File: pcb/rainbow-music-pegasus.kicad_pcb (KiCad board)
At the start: 2 copper layers, 138 x 30.5 mm, 88 parts, among them J1 USB_B_Micro, J2 Conn_02x03_Odd_Even, SW1 SW_SPDT, U1 ESP32-C3-MINI-1, U2 OPA344NA, U3 TLV75533PDBV

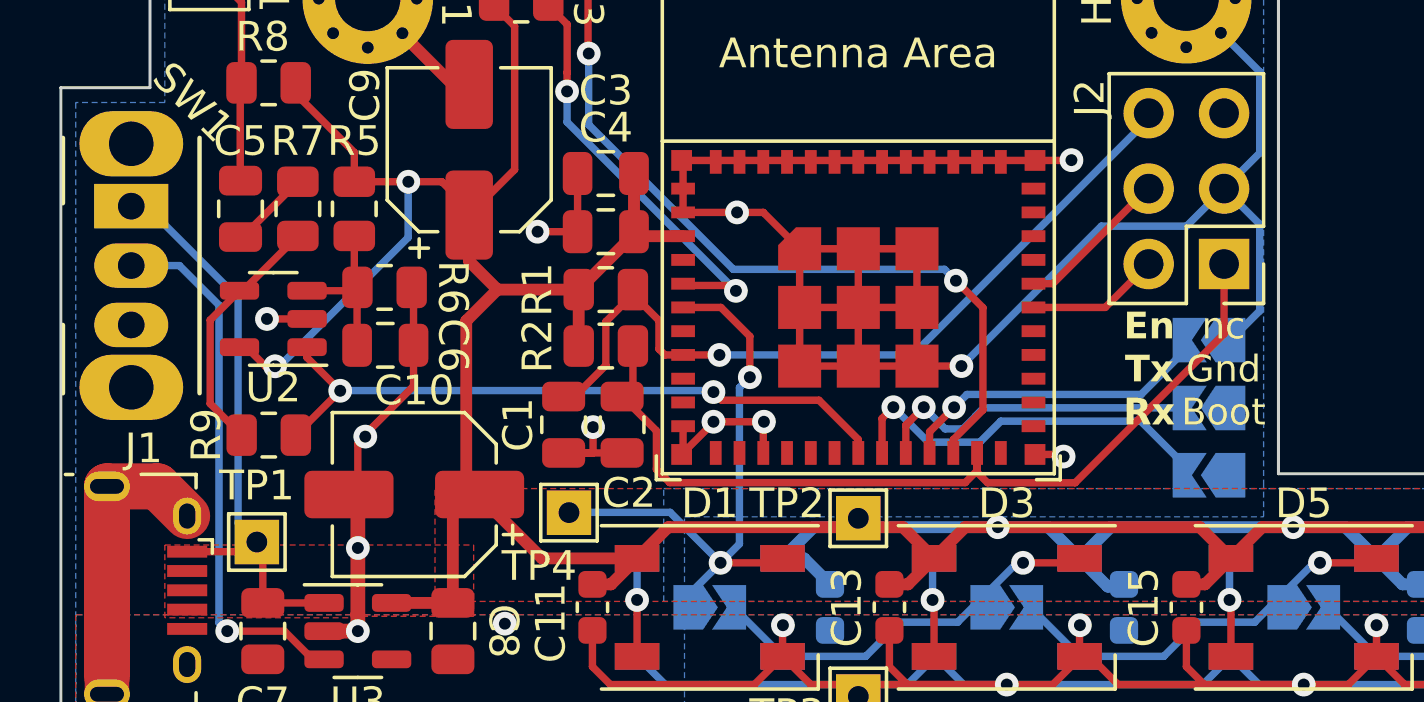
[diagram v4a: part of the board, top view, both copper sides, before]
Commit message: Missed a decoupling capacitor at U2; added as C35
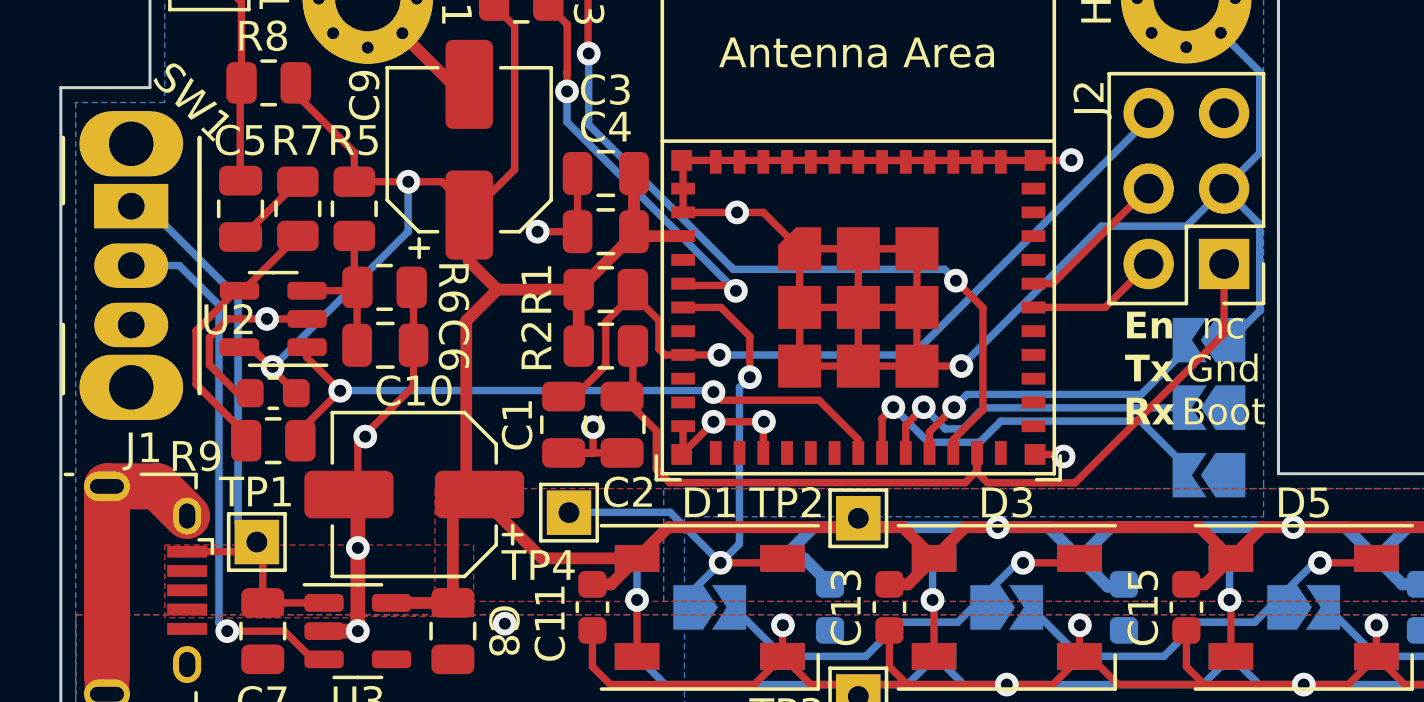
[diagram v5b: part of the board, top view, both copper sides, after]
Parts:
- added C35: 0.1uF, Capacitor_SMD:C_0603_1608Metric, F.Cu at (91.1, 93.4)
- moved R9 0.24 mm to (91.1, 95.0)
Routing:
- net GND: track 413.6 -> 418.5 mm
- net +3.3V: track 351.1 -> 352.2 mm

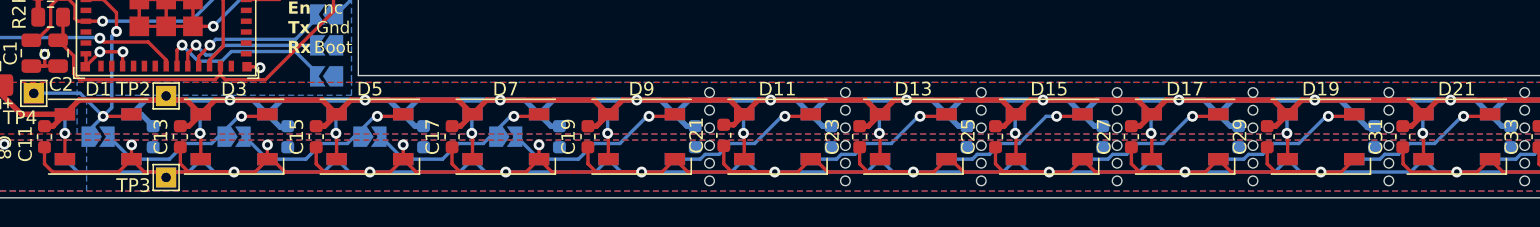
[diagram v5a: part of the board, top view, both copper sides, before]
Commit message: Footprint verification done, ready for first production run!
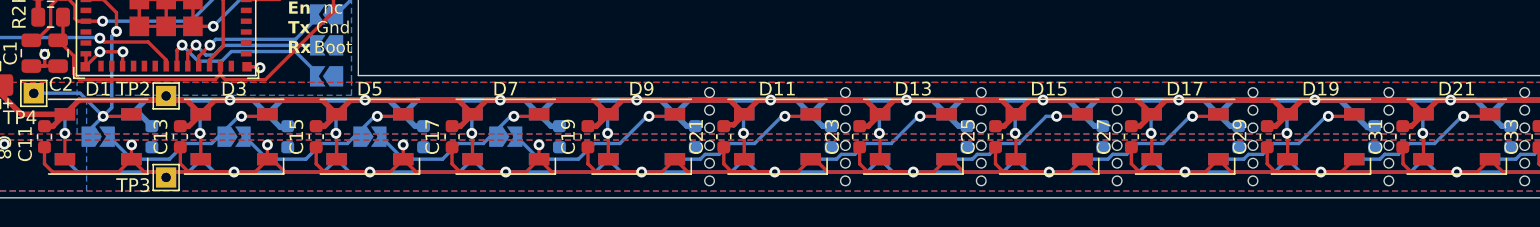
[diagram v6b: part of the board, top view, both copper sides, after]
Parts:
- moved C12 0.10 mm to (109.7, 100.6)
- moved C21 0.10 mm to (151.8, 100.6)
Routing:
- net GND: track 418.5 -> 428.5 mm
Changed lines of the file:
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@@
     )
     (pad_to_mask_clearance 0)
-    (grid_origin 95.8475 96.8)
+    (grid_origin 119.7475 100.6)
     (pcbplotparams
       (layerselection 0x00010fc_ffffffff)
@@
   )
   (footprint "Capacitor_SMD:C_0603_1608Metric" (layer "F.Cu")
-    (at 151.8475 100.5 90)
+    (at 151.8475 100.6 90)
     (descr "Capacitor SMD 0603 (1608 Metric), square (rectangular) end terminal, IPC_7351 nominal, (Body size source: IPC-SM-782 page 76, https://www.pcb-3d.com/wordpress/wp-content/uploads/ipc-sm-782a_amendment_1_and_2.pdf), generated with kicad-footprint-generator")
     (tags "capacitor")
@@
   )
   (footprint "Jumper:SolderJumper-2_P1.3mm_Open_TrianglePad1.0x1.5mm" (layer "B.Cu")
-    (at 105.7975 100.6)
+    (at 105.8 100.6)
     (descr "SMD Solder Jumper, 1x1.5mm Triangular Pads, 0.3mm gap, open")
     (tags "solder jumper open")
@@
   )
   (footprint "Capacitor_SMD:C_0603_1608Metric" (layer "B.Cu")
-    (at 109.8475 100.6 90)
+    (at 109.7475 100.6 90)
     (descr "Capacitor SMD 0603 (1608 Metric), square (rectangular) end terminal, IPC_7351 nominal, (Body size source: IPC-SM-782 page 76, https://www.pcb-3d.com/wordpress/wp-content/uploads/ipc-sm-782a_amendment_1_and_2.pdf), generated with kicad-footprint-generator")
     (tags "capacitor")
@@
   (segment (start 138.25 101.200498) (end 138.25 102.25) (width 0.25) (layer "F.Cu") (net 1))
   (segment (start 131.8475 101.375) (end 131.8475 102.5975) (width 0.25) (layer "F.Cu") (net 1))
+  (segment (start 195.8 103.2) (end 205.8 103.2) (width 0.25) (layer "F.Cu") (net 1))
   (segment (start 132.45 103.2) (end 135.8 103.2) (width 0.25) (layer "F.Cu") (net 1))
   (segment (start 104.85 85.55) (end 116.75 85.55) (width 0.25) (layer "F.Cu") (net 1))
@@
   (segment (start 147.2 97.9) (end 148.25 98.95) (width 0.4) (layer "B.Cu") (net 4))
   (segment (start 149.3 97.9) (end 150.71303 97.9) (width 0.4) (layer "B.Cu") (net 4))
-  (segment (start 109.8475 99.825) (end 108.9725 98.95) (width 0.4) (layer "B.Cu") (net 4))
   (segment (start 199.225 99.925) (end 198.25 98.95) (width 0.4) (layer "B.Cu") (net 4))
   (segment (start 179.3 97.9) (end 180.71303 97.9) (width 0.4) (layer "B.Cu") (net 4))
@@
   (segment (start 157.2 97.9) (end 158.25 98.95) (width 0.4) (layer "B.Cu") (net 4))
   (segment (start 170.71303 97.9) (end 170.776699 97.91335) (width 0.4) (layer "B.Cu") (net 4))
-  (segment (start 108.9725 98.95) (end 108.25 98.95) (width 0.4) (layer "B.Cu") (net 4))
   (segment (start 167.2 97.9) (end 168.25 98.95) (width 0.4) (layer "B.Cu") (net 4))
   (segment (start 179.7475 99.825) (end 179.125 99.825) (width 0.4) (layer "B.Cu") (net 4))
@@
   (segment (start 168.25 98.95) (end 169.3 97.9) (width 0.4) (layer "B.Cu") (net 4))
   (segment (start 215.3475 97.9) (end 210.883805 97.9) (width 0.4) (layer "B.Cu") (net 4))
+  (segment (start 109.75 99.825) (end 108.875 98.95) (width 0.4) (layer "B.Cu") (net 4))
   (segment (start 200.883805 97.9) (end 200.776699 97.91335) (width 0.4) (layer "B.Cu") (net 4))
   (segment (start 149.7475 99.825) (end 149.125 99.825) (width 0.4) (layer "B.Cu") (net 4))
@@
   (segment (start 119.7475 99.825) (end 119.7475 99.9) (width 0.4) (layer "B.Cu") (net 4))
   (segment (start 187.2 97.9) (end 188.25 98.95) (width 0.4) (layer "B.Cu") (net 4))
+  (segment (start 108.875 98.95) (end 108.25 98.95) (width 0.4) (layer "B.Cu") (net 4))
   (segment (start 150.71303 97.9) (end 150.776699 97.91335) (width 0.4) (layer "B.Cu") (net 4))
   (segment (start 207.2 97.9) (end 208.25 98.95) (width 0.4) (layer "B.Cu") (net 4))

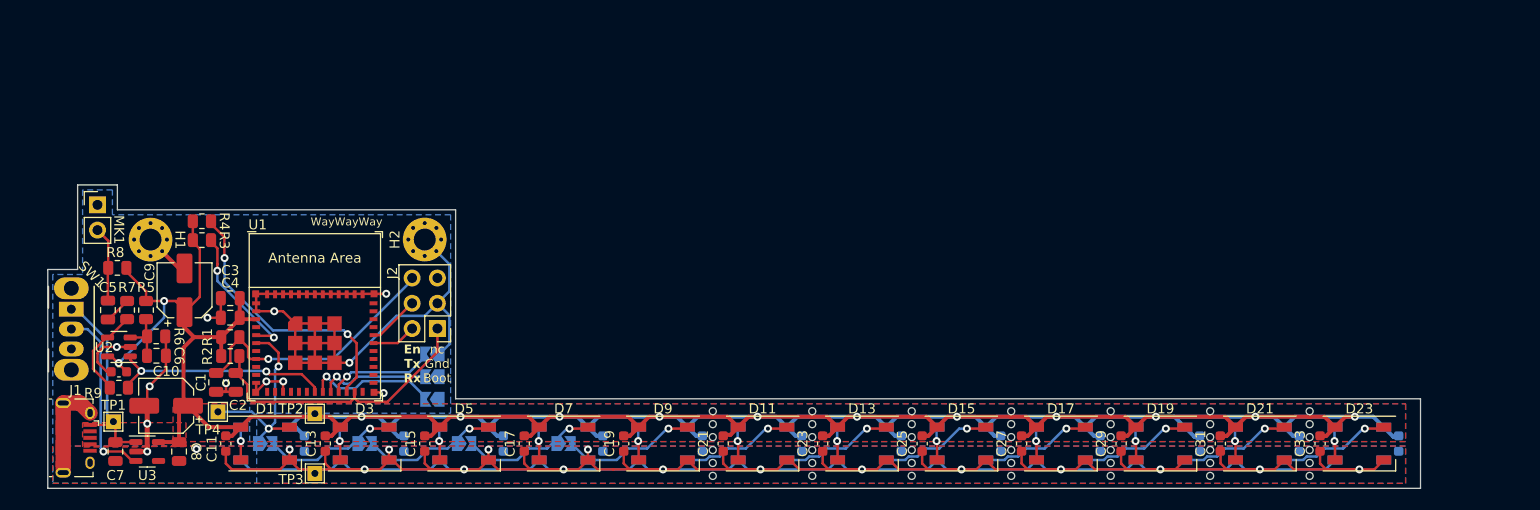
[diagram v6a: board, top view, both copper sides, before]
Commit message: Added Battery charging module and a new mode-setting button
Also found 3d models for the microphone, switch, USB components
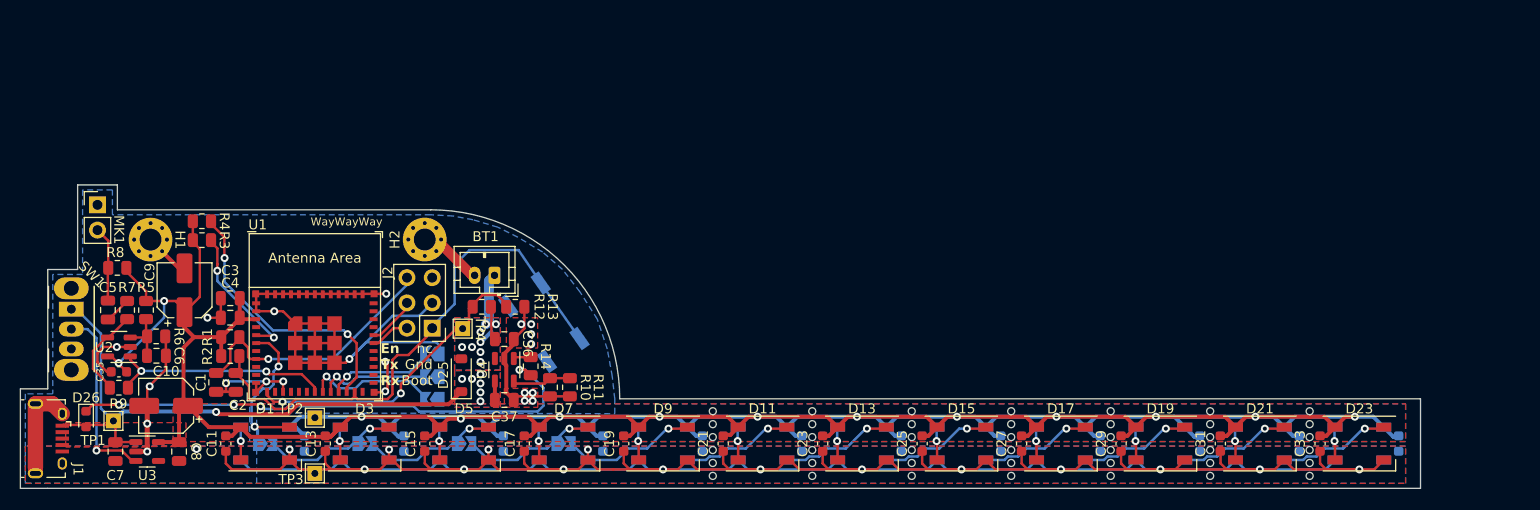
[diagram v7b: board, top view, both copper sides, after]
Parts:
- added BT1: Battery_Cell, Connector_JST:JST_PH_B2B-PH-K_1x02_P2.00mm_Vertical, F.Cu at (128.9, 83.7)
- added C36: 4.7uF, Capacitor_SMD:C_0805_2012Metric, F.Cu at (129.8, 90.1)
- added C37: 4.7uF, Capacitor_SMD:C_0805_2012Metric, F.Cu at (129.8, 96.2)
- added D25: MBR120, Diode_SMD:D_SOD-123, F.Cu at (125.5, 93.7)
- added D26: LED, LED_SMD:LED_0603_1608Metric, F.Cu at (87.8, 98.1)
- added R10: 10k, Resistor_SMD:R_0805_2012Metric, F.Cu at (134.4, 94.9)
- added R11: 10k, Resistor_SMD:R_0805_2012Metric, F.Cu at (136.4, 94.9)
- added R12: 100k, Resistor_SMD:R_0805_2012Metric, F.Cu at (127.6, 86.8)
- added R13: 100k, Resistor_SMD:R_0805_2012Metric, F.Cu at (130.9, 86.8)
- added R14: 1k, Resistor_SMD:R_0805_2012Metric, F.Cu at (132.5, 92.8)
- added SW2: SW_Push, Button_Switch_SMD:SW_SPST_EVQQ2, B.Cu at (133.8, 88.4)
- added U4: MCP73831-2-OT, Package_TO_SOT_SMD:SOT-23-5, F.Cu at (129.8, 93.2)
- moved TP4 26.0 mm to (125.7, 89.0)
- moved J1 2.79 mm to (83.9, 100.1)
- moved J2 0.52 mm to (122.6, 89.0)
- moved TP2 0.40 mm to (110.8, 98.0)
- moved TP1 0.08 mm to (90.5, 98.3)
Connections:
- net Net-(J1-VBUS) renamed VBUS
- TP4 pad 1: /RGB_Data -> /Batt_Level
- U1 pad 12: unconnected-(U1-GPIO0/ADC1_CH0/XTAL_32K_P-Pad12) -> /Batt_Level
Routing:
- net Net-(D26-K): track 0.00 -> 53.3 mm, vias 0 -> 4
- net VBUS: track 19.9 -> 61.1 mm, vias 0 -> 7
- net /Batt_Level: track 0.00 -> 31.1 mm, vias 0 -> 2
- net GND: track 428.5 -> 455.3 mm, vias 28 -> 37
- net /Boot: track 30.1 -> 55.7 mm
- net +BATT: track 0.00 -> 11.4 mm, vias 0 -> 8
- net Net-(U4-PROG): track 0.00 -> 5.97 mm
- net /RGB_Data: track 20.6 -> 17.1 mm
- net Net-(U4-STAT): track 0.00 -> 1.76 mm
- net /Reset: track 27.2 -> 27.8 mm
- net /RXD: track 4.48 -> 3.98 mm
- added copper zone on B.Cu, net +BATT
- added copper zone on F.Cu, net +BATT
- added copper zone on B.Cu, net VBUS
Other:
- board size 138 x 30.5 mm -> 140.8 x 30.5 mm
- board text added: "Set Mode (See website)"
- board text added: "v1.1"
- board text removed: "v1"

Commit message: Finalized battery design including charging status lights
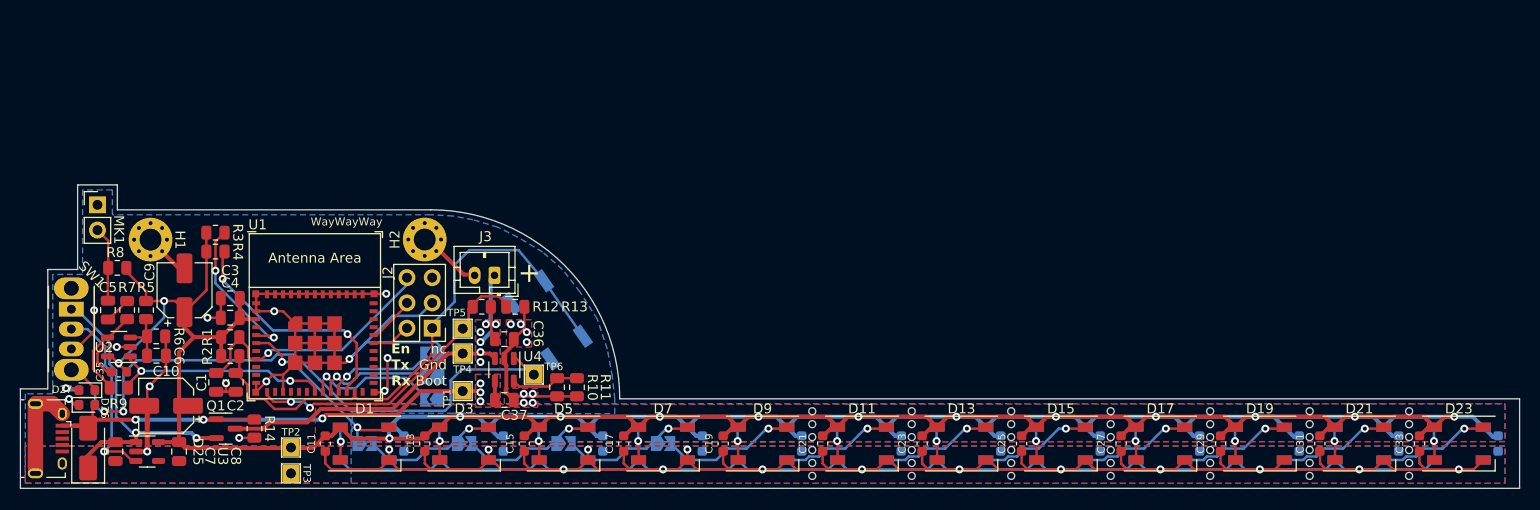
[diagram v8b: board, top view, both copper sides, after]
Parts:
- added D27: GREEN, LED_SMD:LED_0603_1608Metric, F.Cu at (87.9, 95.2)
- added Q1: DMG3415U, Package_TO_SOT_SMD:SOT-23, F.Cu at (101.8, 99.1)
- added R14: 100k, Resistor_SMD:R_0805_2012Metric, F.Cu at (104.7, 99.1)
- added R15: 500, Resistor_SMD:R_0603_1608Metric, B.Cu at (87.9, 96.7)
- added TP5: TestPoint, TestPoint:TestPoint_THTPad_1.5x1.5mm_Drill0.7mm, F.Cu at (125.7, 89.0)
- added TP6: TestPoint, TestPoint:TestPoint_THTPad_1.5x1.5mm_Drill0.7mm, F.Cu at (132.8, 93.7)
- D25: value MBR120 -> CDBA540; footprint Diode_SMD:D_SOD-123 -> Diode_SMD:D_SMA
- D26: value LED -> RED
- J3: renamed from BT1; value Battery_Cell -> B2B-PH-K-S
- R16: renamed from R14; value 1k -> 500; footprint Resistor_SMD:R_0805_2012Metric -> Resistor_SMD:R_0603_1608Metric; moved to B.Cu
- SW2: value SW_Push -> EVQQ2
- moved R16 44.7 mm to (87.9, 95.2), turned to 0 degrees
- moved D25 38.2 mm to (88.0, 101.0)
- moved TP1 35.2 mm to (125.7, 95.3)
- moved D5 10.0 mm to (135.8, 100.6)
- moved D6 10.0 mm to (135.8, 100.6)
- moved JP3 10.0 mm to (135.8, 100.6)
- moved C11 10.0 mm to (111.8, 100.6)
- moved C12 10.0 mm to (119.7, 100.6)
- moved C13 10.0 mm to (121.8, 100.6)
- moved C14 10.0 mm to (129.7, 100.6)
- moved C15 10.0 mm to (131.8, 100.6)
- moved C16 10.0 mm to (139.7, 100.6)
- moved C17 10.0 mm to (141.8, 100.6)
- moved C18 10.0 mm to (149.7, 100.6)
- moved C19 10.0 mm to (151.8, 100.6)
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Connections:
- C7 pad 2: VBUS -> Net-(D25-K)
- D25 pad 1: VBUS -> Net-(D25-K)
- D25 pad 2: +BATT -> VBUS
- R16 pad 1: Net-(D26-K) -> Net-(D27-A)
- SW1 pad 1: VBUS -> Net-(D25-K)
- TP4 pad 1: /Batt_Level -> +BATT
- U3 pad 1: VBUS -> Net-(D25-K)
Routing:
- net Net-(U4-STAT): track 1.76 -> 59.2 mm, vias 0 -> 2
- net Net-(D26-K): track 53.3 -> 2.83 mm, vias 4 -> 1
- net Net-(D25-K): track 0.00 -> 31.0 mm, vias 0 -> 2
- net +BATT: track 11.4 -> 40.1 mm, vias 8 -> 6
- net +3.3V: track 352.1 -> 360.3 mm, vias 13 -> 14
- net GND: track 455.3 -> 462.3 mm, vias 37 -> 35
- net VBUS: track 61.1 -> 55.4 mm, vias 7 -> 6
- net Net-(U1-GPIO8): track 27.8 -> 24.3 mm
- net Net-(D27-A): track 0.00 -> 2.77 mm, vias 0 -> 1
- net /RGB_Data: track 17.1 -> 19.1 mm
- net Net-(U1-GPIO2/ADC1_CH2): track 14.3 -> 15.5 mm
- net Net-(U4-PROG): track 5.97 -> 6.92 mm
- net /Reset: track 27.8 -> 27.0 mm
- net /Boot: track 55.7 -> 55.0 mm
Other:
- board size 140.8 x 30.5 mm -> 150.7 x 30.5 mm
- board text added: "+"
